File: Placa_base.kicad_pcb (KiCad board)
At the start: 2 copper layers, 200 x 100 mm, 214 parts, among them J1 SWD/STLINK, J10 Interfaz con entradas digital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, J11 I2C1, J12 USART6, J13 CAN1, J14 SPI1, J15 Conn_02x08_Odd_Even, J2 Bateria, J3 Entrada 24V, J4 RS-485, J5 TV_6V, J6 AN1, J7 AN2, J8 Micro_SD_Card_Det_Hirose_DM3AT, J9 Salidas 5V, Q1 MMBT3904, Q2 MMBT3904, Q3 MMBT3904, Q4 AO3401, Q5 AO3401, SW1 SW_Push, SW2 SW_Push, SW3 SW_Push, U1 STM32F407VGTx, U10 MCP6L04T-E/ST, U11 74HCT541, U2 DC-DC_Step-Down, U3 AZ1117-3.3, U4 AZ1117-3.3, U5 RFM-0505S, U6 ISO1412, U7 NodeMCU_1.0_(ESP-12E), U8 SIM800L_modulo, U9 Modulo_A6_Mini, Y1 32.768KHz, Y2 8MHz

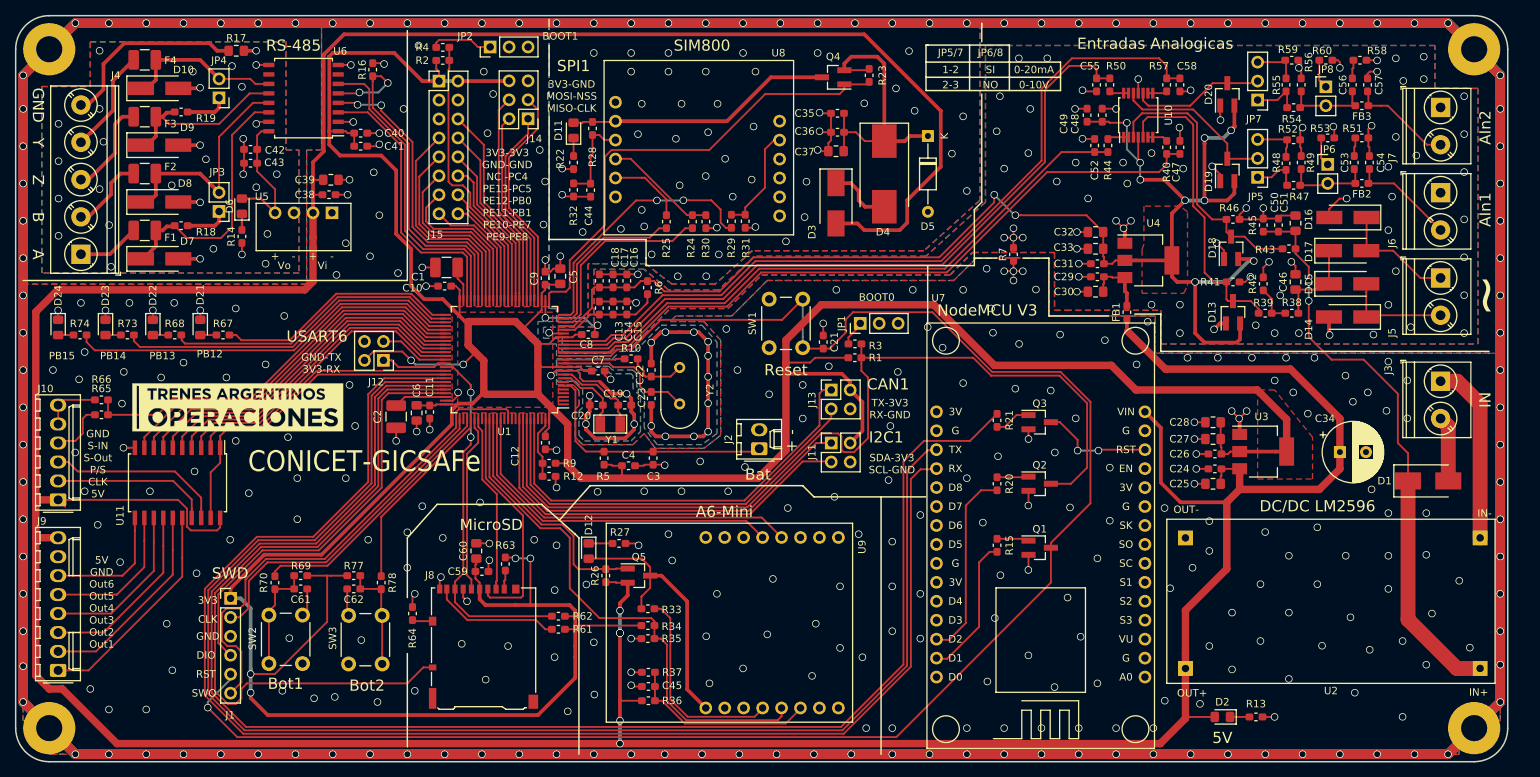
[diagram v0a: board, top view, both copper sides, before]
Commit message: Modificaciones menores en esquemático y PCB
Se reemplazó I2C3 por USART6 (debug), se agregaron pull-ups en I2C1, reducción de agujeros de vías a 0.5mm y actualización de labels en esquemático.
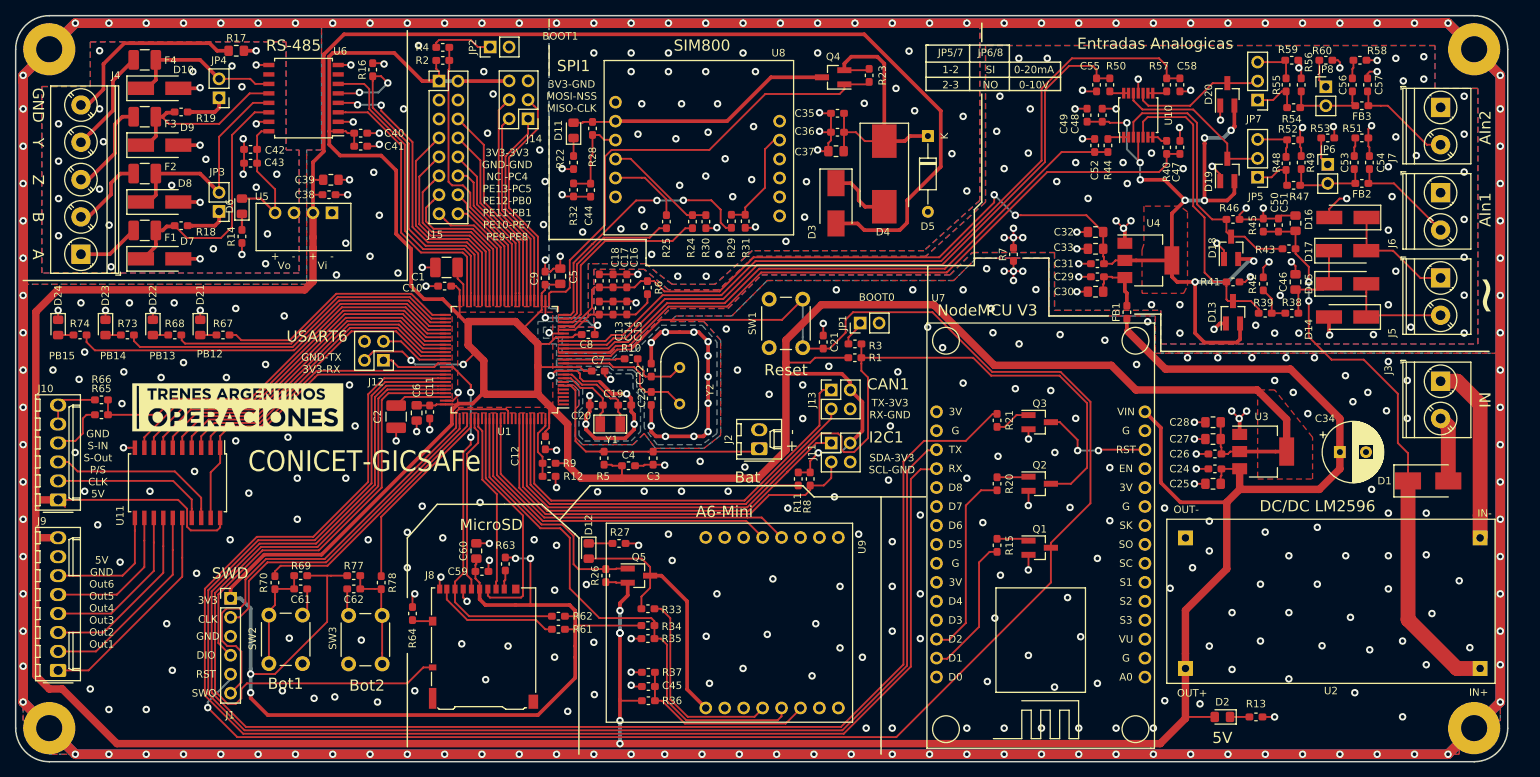
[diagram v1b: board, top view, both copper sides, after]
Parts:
- added R11: 4K7, Resistor_SMD:R_0603_1608Metric_Pad1.05x0.95mm_HandSolder, F.Cu at (174.9, 102.1)
- added R8: 4K7, Resistor_SMD:R_0603_1608Metric_Pad1.05x0.95mm_HandSolder, F.Cu at (176.5, 102.1)
- JP1, JP2: value Jumper_3_Open -> Jumper_2_Open; footprint Connector_PinHeader_2.54mm:PinHeader_1x03_P2.54mm_Vertical -> Connector_PinHeader_2.54mm:PinHeader_1x02_P2.54mm_Vertical
- moved JP1 0.05 mm to (183.2, 81.2)
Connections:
- net /PA0 renamed /USART4_TX
- net /PA1 renamed /USART4_RX
- net /PA10 renamed /USART1_RX
- net /PA11 renamed /Reset_ESP
- net /PA12 renamed /uSD_Det
- net /PA2 renamed /S800_DTR
- net /PA3 renamed /S800_ON
- net /PA4 renamed /SPI1_NSS
- net /PA5 renamed /SPI1_CK
- net /PA6 renamed /SPI1_MISO
- net /PA7 renamed /SPI1_MOSI
- net /PA8 renamed /OUT_EN
- net /PA9 renamed /USART1_TX
- net /PB0 renamed /EXP_PIN5
- net /PB1 renamed /EXP_PIN7
- net /PB10 renamed /RS-485_D
- net /PB11 renamed /RS-485_R
- net /PB6 renamed /I2C1_SCL
- net /PB7 renamed /I2C1_SDA
- net /PB8 renamed /CAN1_RX
- net /PB9 renamed /CAN1_TX
- net /PC12 renamed /uSD_CK
- net /PC4 renamed /EXP_PIN1
- net /PC5 renamed /EXP_PIN3
- net /PC6 renamed /USART6_TX
- net /PC7 renamed /USART6_RX
- net /PC8 renamed /uSD_D0
- net /PC9 renamed /IN_P-S
- net /PD0 renamed /uSD_CD
- net /PD10 renamed /OUT_5
- net /PD11 renamed /OUT_4
- net /PD12 renamed /OUT_3
- net /PD13 renamed /OUT_2
- net /PD14 renamed /OUT_1
- net /PD15 renamed /IN_CLK
- net /PD2 renamed /uSD_Cmd
- net /PD3 renamed /A6_INT
- net /PD4 renamed /A6_ON
- net /PD5 renamed /USART2_TX
- net /PD6 renamed /USART2_RX
- net /PD8 renamed /IN_Read
- net /PD9 renamed /OUT_6
- net /PE10 renamed /EXP_PIN8
- net /PE11 renamed /EXP_PIN6
- net /PE12 renamed /EXP_PIN4
- net /PE13 renamed /EXP_PIN2
- net /PE14 renamed /RS-485_RE
- net /PE15 renamed /RS-485_DE
- net /PE7 renamed /EXP_PIN9
- net /PE8 renamed /EXP_PIN11
- net /PE9 renamed /EXP_PIN10
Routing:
- net VDD: track 540.5 -> 550.0 mm, vias 6 -> 7
- net /I2C1_SDA: track 55.6 -> 59.0 mm
- net /I2C1_SCL: track 55.5 -> 57.2 mm
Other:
- net class Default: via_drill 0.8 -> 0.5
- rule via_min_drill: 0.8 -> 0.5

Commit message: Reemplazo de todos los footprints
Se reemplazaron todos los footprints para hacer soldadura por horno y se acomodó nuevamente la serigrafía.
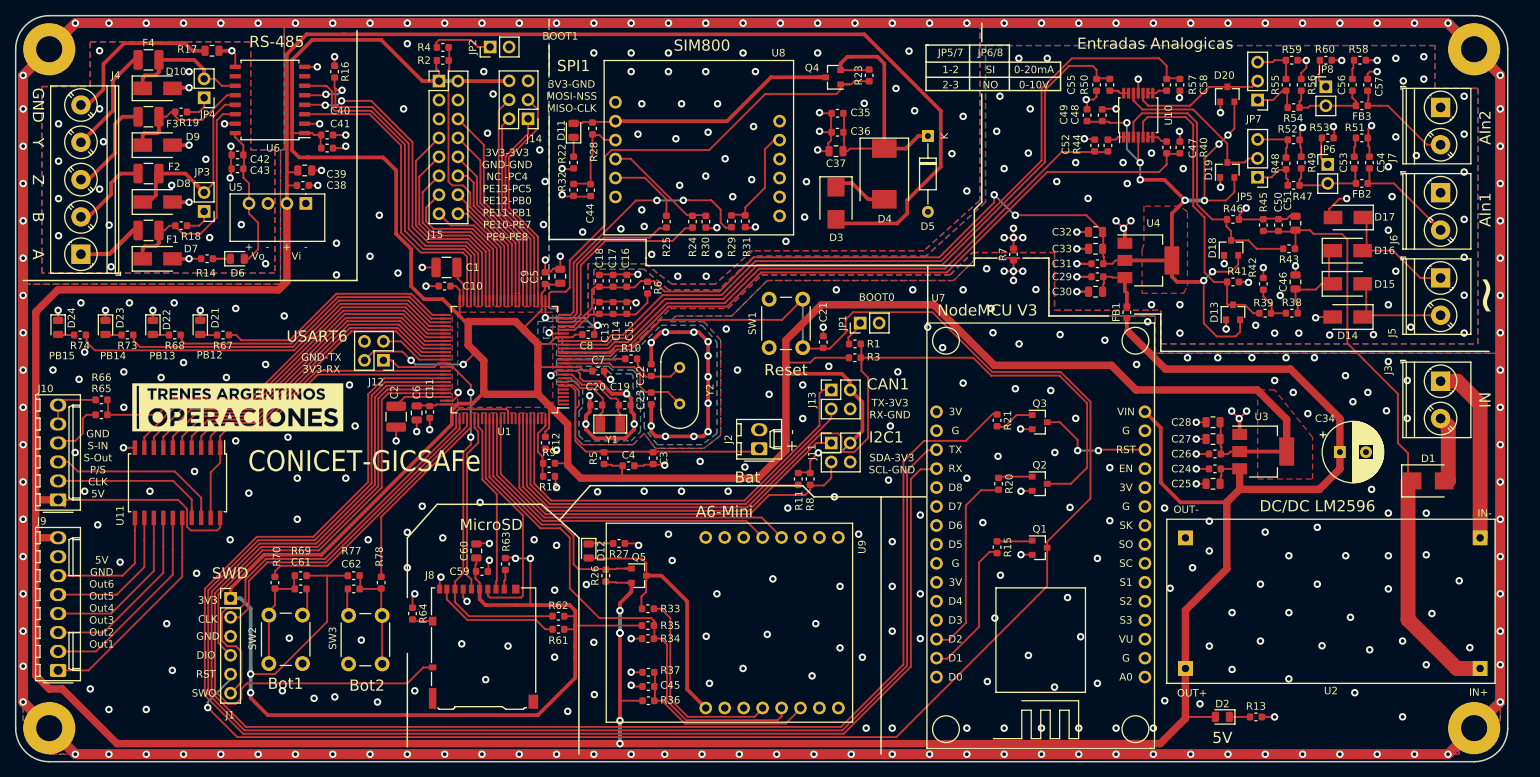
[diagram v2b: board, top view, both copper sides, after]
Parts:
- C1, C2: footprint Capacitor_SMD:C_1210_3225Metric_Pad1.42x2.65mm_HandSolder -> Capacitor_SMD:C_1210_3225Metric
- C10, C11, C12, C13, C14, C15, C16, C17, C18, C19, C20, C21, C22, C23, C24, C26, C29, C3, C31, C35, C36, C38, C4, C40, C41, C42, C43, C44, C45, C47, C48, C49, C50, C52, C53, C54, C55, C56, C57, C58, C59, C61, C62, C7, C8, C9: footprint Capacitor_SMD:C_0603_1608Metric_Pad1.05x0.95mm_HandSolder -> Capacitor_SMD:C_0603_1608Metric
- C25, C27, C28, C30, C32, C33, C37, C39, C46, C5, C51, C6, C60: footprint Capacitor_SMD:C_0805_2012Metric_Pad1.15x1.40mm_HandSolder -> Capacitor_SMD:C_0805_2012Metric
- D1, D3: footprint Diode_SMD:D_SMB_Handsoldering -> Diode_SMD:D_SMB
- D10, D14, D15, D16, D17, D7, D8, D9: footprint Diode_SMD:D_SMA_Handsoldering -> Diode_SMD:D_SMA
- D11, D12, D2, D21, D22, D23, D24, D6: footprint LED_SMD:LED_0805_2012Metric_Pad1.15x1.40mm_HandSolder -> LED_SMD:LED_0805_2012Metric
- D13, D18, D19, D20, Q1, Q2, Q3, Q4, Q5: footprint Package_TO_SOT_SMD:SOT-23_Handsoldering -> Package_TO_SOT_SMD:SOT-23
- D4: footprint Diode_SMD:D_SMC_Handsoldering -> Diode_SMD:D_SMC
- F1, F2, F3, F4: footprint Resistor_SMD:R_1210_3225Metric_Pad1.42x2.65mm_HandSolder -> Resistor_SMD:R_1210_3225Metric
- FB1, FB2, FB3, R1, R10, R11, R12, R13, R14, R15, R16, R18, R19, R2, R20, R21, R22, R23, R24, R25, R26, R27, R28, R29, R3, R30, R31, R32, R33, R34, R35, R36, R37, R38, R39, R4, R40, R41, R42, R43, R44, R45, R46, R47, R48, R49, R5, R50, R51, R52, R53, R54, R55, R56, R57, R58, R59, R6, R60, R61, R62, R63, R64, R65, R66, R67, R68, R69, R7, R70, R73, R74, R77, R78, R8, R9: footprint Resistor_SMD:R_0603_1608Metric_Pad1.05x0.95mm_HandSolder -> Resistor_SMD:R_0603_1608Metric
- R17: footprint Resistor_SMD:R_0805_2012Metric_Pad1.15x1.40mm_HandSolder -> Resistor_SMD:R_0805_2012Metric
- moved D6 7.07 mm to (99.7, 72.6), turned to 0 degrees
- moved R14 5.55 mm to (95.7, 72.6), turned to 0 degrees
- moved R16 5.11 mm to (112.8, 47.5)
- moved C40 4.51 mm to (111.8, 56.0)
- moved C41 4.51 mm to (111.8, 57.8)
- moved U6 4.51 mm to (104.1, 51.3)
- moved C38 3.72 mm to (108.5, 62.8)
- moved C39 3.72 mm to (108.8, 60.8)
- moved U5 3.72 mm to (108.9, 65.2)
- moved R17 3.25 mm to (96.3, 44.7)
- moved JP3 2.00 mm to (95.3, 66.2)
- moved JP4 2.00 mm to (95.3, 51.0)
- moved C42 1.90 mm to (99.7, 58.7)
- moved C43 1.90 mm to (99.7, 60.5)
- moved F1 0.50 mm to (87.8, 68.8)
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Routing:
- net VDD: track 550.0 -> 562.3 mm
- net Net-(F1-Pad1): track 8.39 -> 14.9 mm
- net VDDA: track 189.0 -> 182.6 mm
- net /RS-485_R: track 38.0 -> 42.4 mm
- net /RS-485_RE: track 40.6 -> 44.9 mm
- net /WiFi/Z: track 25.1 -> 20.9 mm
- net /RS-485_D: track 41.7 -> 45.8 mm
- net /WiFi/A: track 35.1 -> 31.3 mm
- net /WiFi/B: track 30.8 -> 27.1 mm
- net /analogico/AIn1: track 77.7 -> 81.0 mm, vias 2 -> 0
- net Net-(J4-Pad5): track 25.6 -> 22.5 mm
- net /WiFi/Y: track 21.6 -> 18.8 mm
- net Earth: track 23.7 -> 21.2 mm, vias 30 -> 24
- net GND: track 1347.6 -> 1345.3 mm, vias 428 -> 427
- net Net-(JP4-Pad1): track 5.78 -> 3.80 mm
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
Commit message: Cambios para reducir PCB
Cambio de nodemcu por wemos y ajuste de todas las pistas
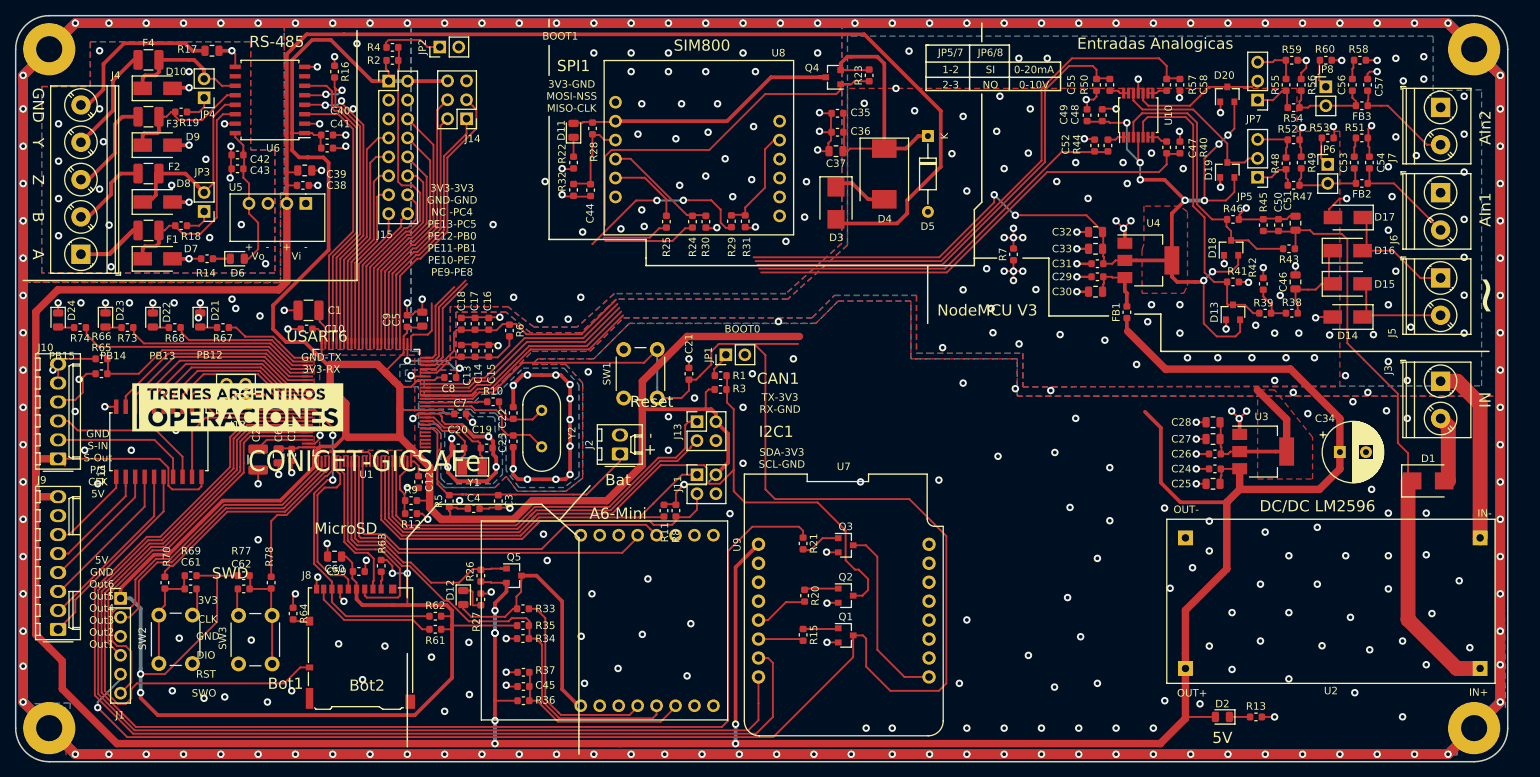
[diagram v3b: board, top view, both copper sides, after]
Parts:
- U7: value NodeMCU_1.0_(ESP-12E) -> WeMos_mini; footprint Propios:NodeMCU1.0(12-E) -> wemos:wemos-d1-mini-with-pin-header-and-connector
- moved Q3 30.8 mm to (181.3, 111.0)
- moved R21 30.8 mm to (175.5, 110.7)
- moved Q2 30.0 mm to (181.3, 117.7)
- moved R20 30.0 mm to (175.8, 117.7)
- moved U7 29.0 mm to (181.0, 119.8), turned to 270 degrees
- moved Q1 28.5 mm to (181.3, 123.1)
- moved R15 28.5 mm to (175.5, 123.0)
- moved C3 21.5 mm to (134.7, 105.1)
- moved C4 21.5 mm to (131.4, 106.1)
- moved R5 21.5 mm to (128.1, 105.1)
- moved SW1 20.6 mm to (156.0, 84.8)
- moved R27 20.0 mm to (132.3, 118.2), turned to 270 degrees
- moved C5 19.4 mm to (124.5, 80.7)
- moved C1 19.4 mm to (109.2, 79.5)
- moved C10 19.4 mm to (109.0, 82.0)
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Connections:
- U7 pad 1: Net-(U7-Pad1) -> +5V
- U7 pad 10: GND -> Net-(U7-Pad10)
- U7 pad 13: Net-(Q3-Pad3) -> Net-(U7-Pad13)
- U7 pad 14: GND -> Net-(U7-Pad14)
- U7 pad 15: +5V -> Net-(U7-Pad15)
- U7 pad 2: Net-(U7-Pad2) -> GND
- U7 pad 5: Net-(U7-Pad5) -> Net-(R20-Pad2)
- U7 pad 6: Net-(U7-Pad6) -> Net-(R15-Pad2)
- U7 pad 7: Net-(U7-Pad7) -> /USART1_TX
- U7 pad 8: Net-(U7-Pad8) -> /USART1_RX
- U7 pad 9: Net-(U7-Pad9) -> Net-(Q3-Pad3)
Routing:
- net VDD: track 562.3 -> 493.1 mm
- net /USART1_RX: track 194.3 -> 150.4 mm
- net /USART1_TX: track 194.4 -> 157.8 mm
- net +5V: track 581.3 -> 611.3 mm, vias 5 -> 7
- net /Reset_ESP: track 203.7 -> 174.0 mm
- net /IN_Read: track 54.5 -> 31.4 mm
- net /NRST: track 243.9 -> 266.6 mm
- net /LED4: track 53.3 -> 32.5 mm
- net /LED3: track 46.7 -> 25.8 mm
- net /LED2: track 40.0 -> 19.2 mm
- net /LED1: track 33.0 -> 12.1 mm
- net /OUT_EN: track 45.1 -> 24.4 mm
- net /OUT_6: track 50.1 -> 29.4 mm
- net /OUT_5: track 48.6 -> 28.0 mm
- net /OUT_3: track 45.7 -> 25.1 mm
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
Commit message: Continuo con la reducción
conecté las pistas faltantes, resta reducir los márgenes y planos de masa.
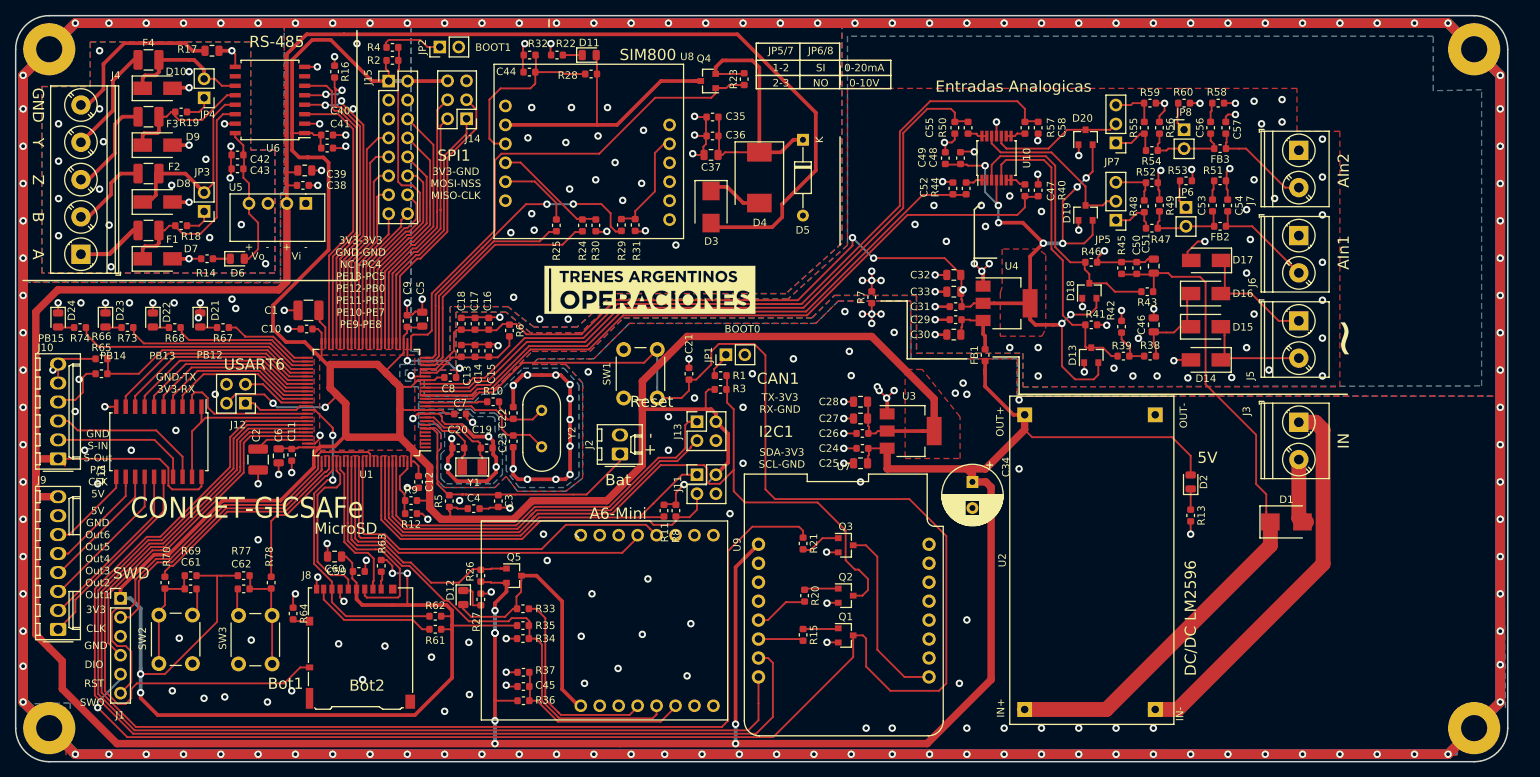
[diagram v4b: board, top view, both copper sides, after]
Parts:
- moved U2 61.3 mm to (205.2, 133.0), turned to 90 degrees
- moved G1 57.5 mm to (155.0, 76.8)
- moved C34 49.4 mm to (198.2, 102.5), turned to 270 degrees
- moved C24 47.3 mm to (183.5, 98.0)
- moved C25 47.3 mm to (183.2, 100.0)
- moved C26 47.3 mm to (183.5, 96.0)
- moved C27 47.3 mm to (183.2, 94.0)
- moved C28 47.3 mm to (183.2, 91.8)
- moved U3 47.3 mm to (190.0, 95.7)
- moved D2 31.8 mm to (227.5, 102.5), turned to 90 degrees
- moved R13 28.4 mm to (227.5, 107.0), turned to 270 degrees
- moved C29 19.9 mm to (196.0, 80.8)
- moved C30 19.9 mm to (195.8, 82.8)
- moved C31 19.9 mm to (196.0, 79.0)
- moved C32 19.9 mm to (195.8, 74.8)
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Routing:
- net +5V: track 611.3 -> 546.7 mm
- net Net-(J3-Pad1): track 24.5 -> 52.2 mm
- net VDD: track 493.1 -> 509.1 mm
- net /analogico/AIn1: track 81.0 -> 95.0 mm
- net Net-(C44-Pad1): track 13.1 -> 26.0 mm
- net /S800_ON: track 57.6 -> 69.1 mm
- net /S800_DTR: track 35.9 -> 42.7 mm
- net /USART4_RX: track 22.7 -> 29.5 mm
- net /USART4_TX: track 26.4 -> 33.2 mm
- net /NRST: track 266.6 -> 259.9 mm
- net Net-(D11-Pad2): track 37.0 -> 38.6 mm
- net /An_In1: track 94.5 -> 94.0 mm
- net VDDA: track 182.6 -> 182.2 mm, vias 11 -> 12
- net GND: track 1344.7 -> 1344.6 mm, vias 368 -> 277
- net GNDA: vias 80 -> 73
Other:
- board text removed: "NodeMCU V3"
